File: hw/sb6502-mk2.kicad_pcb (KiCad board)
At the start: 2 copper layers, 160 x 120 mm, 66 parts, among them J1 Conn_01x03_Pin, J10 Conn_01x04_Socket, J11 Conn_01x04_Socket, J12 Conn_01x08_Socket, J13 Conn_01x08_Socket, J14 Conn_01x08_Socket, J15 Conn_01x08_Socket, J16 Conn_01x08_Socket, J17 Conn_01x04_Socket, J18 Conn_01x04_Socket, J19 Conn_01x02_Socket, J2 Conn_01x03_Pin, J20 Barrel_Jack, J21 Conn_01x02_Socket, J3 DE9_Receptacle, J4 Conn_01x08_Socket, J5 Conn_01x02_Socket, J6 Conn_01x08_Socket, J7 Conn_01x02_Socket, J8 Conn_01x07_Socket, J9 Conn_01x16_Socket, SW1 SW_Push, U1 TC1213, U10 W65C22NxP, U11 74HC138, U2 W65C02SxP, U3 74HC273, U4 ATF22V10, U5 ATF22V10, U6 HM628128, U7 AT28C256, U8 MC68B50, U9 MAX232, X1 1.8432 MHz

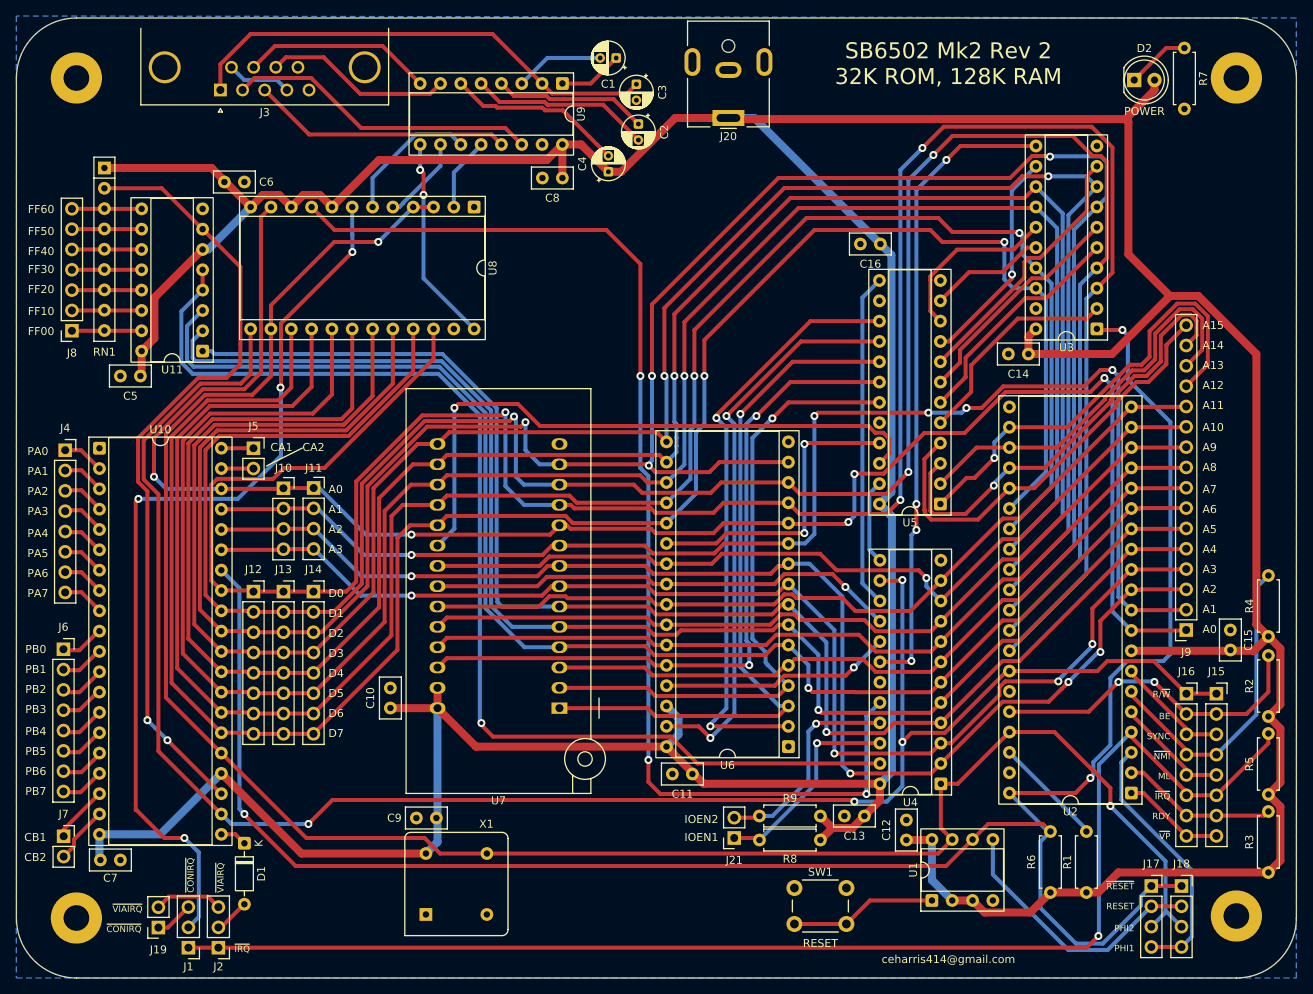
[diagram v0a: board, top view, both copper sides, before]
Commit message: additional pin sockets
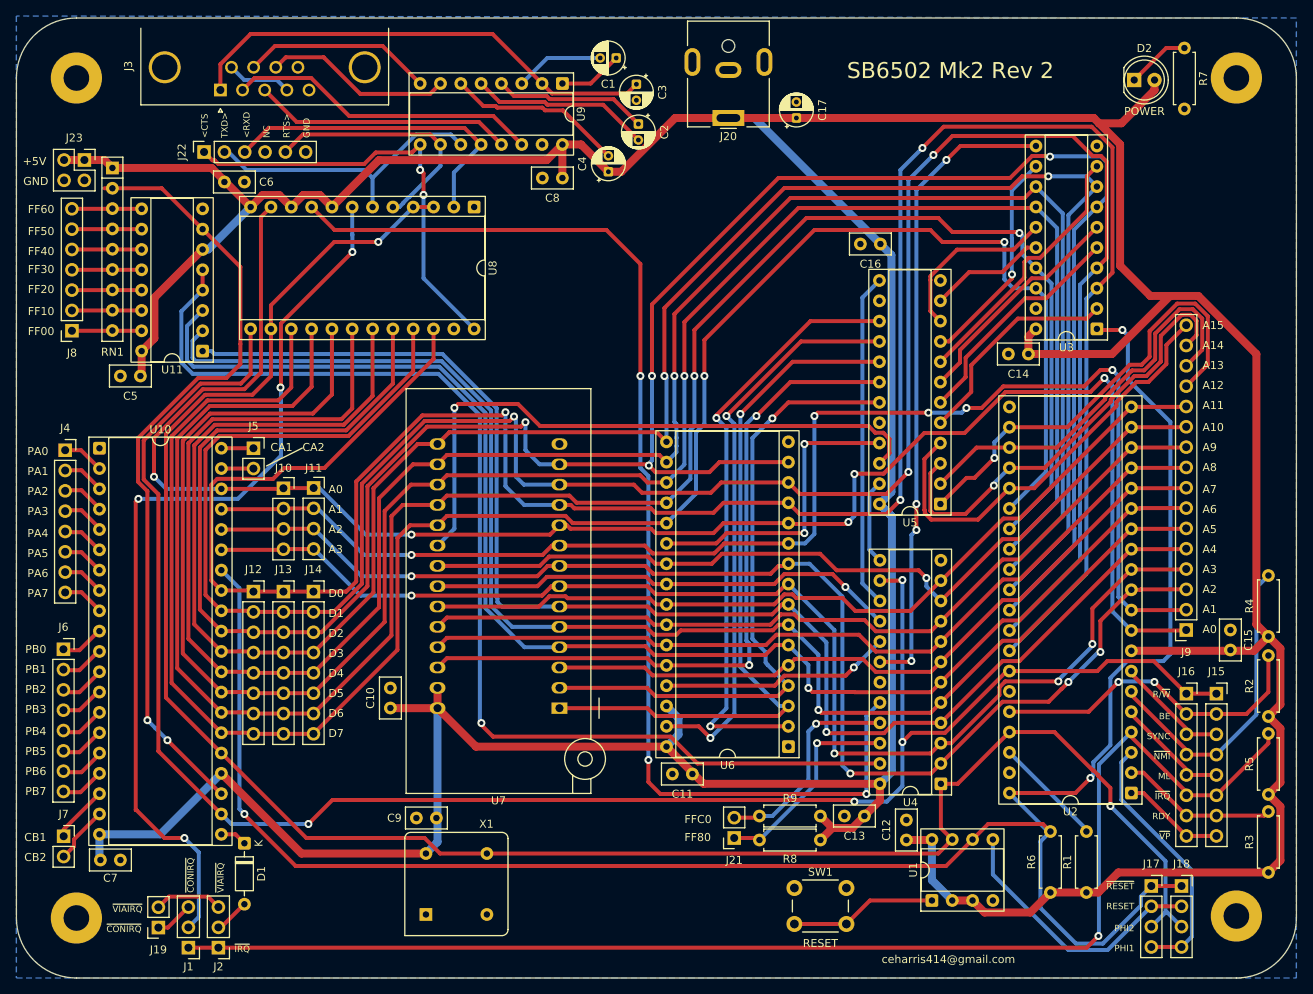
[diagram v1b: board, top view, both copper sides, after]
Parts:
- added C17: 10µF, Capacitor_THT:CP_Radial_D4.0mm_P2.00mm, F.Cu at (122.5, 37.5)
- added J22: Conn_01x06_Socket, Connector_PinSocket_2.54mm:PinSocket_1x06_P2.54mm_Vertical, F.Cu at (48.5, 41.8)
- added J23: Conn_02x02_Counter_Clockwise, Connector_PinSocket_2.54mm:PinSocket_2x02_P2.54mm_Vertical, F.Cu at (33.5, 42.8)
- moved RN1 1.00 mm to (37.0, 43.7)
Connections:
- net Net-(U8-Rx_Data) renamed /IO/RXD
- net Net-(U8-Tx_Data) renamed /IO/TXD
- net Net-(U8-~{CTS}) renamed /IO/CTS
- net Net-(U8-~{RTS}) renamed /IO/RTS
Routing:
- net /IO/RXD: track 9.23 -> 40.9 mm
- net /IO/CTS: track 26.1 -> 54.8 mm
- net /IO/RTS: track 10.8 -> 31.6 mm
- net /IO/TXD: track 17.4 -> 37.3 mm
- net VCC: track 636.4 -> 645.0 mm
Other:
- board text added: "+5V"
- board text added: "<CTS"
- board text added: "<RXD"
- board text added: "FF80"
- board text added: "FFC0"
- board text added: "GND"
- board text added: "NC"
- board text added: "RTS>"
- board text added: "SB6502 Mk2 Rev 2"
- board text added: "TXD>"
- board text removed: "IOEN1"
- board text removed: "IOEN2"
- board text removed: "SB6502 Mk2 Rev 2 32K ROM, 128K RAM"

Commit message: remove unnecessary pullups
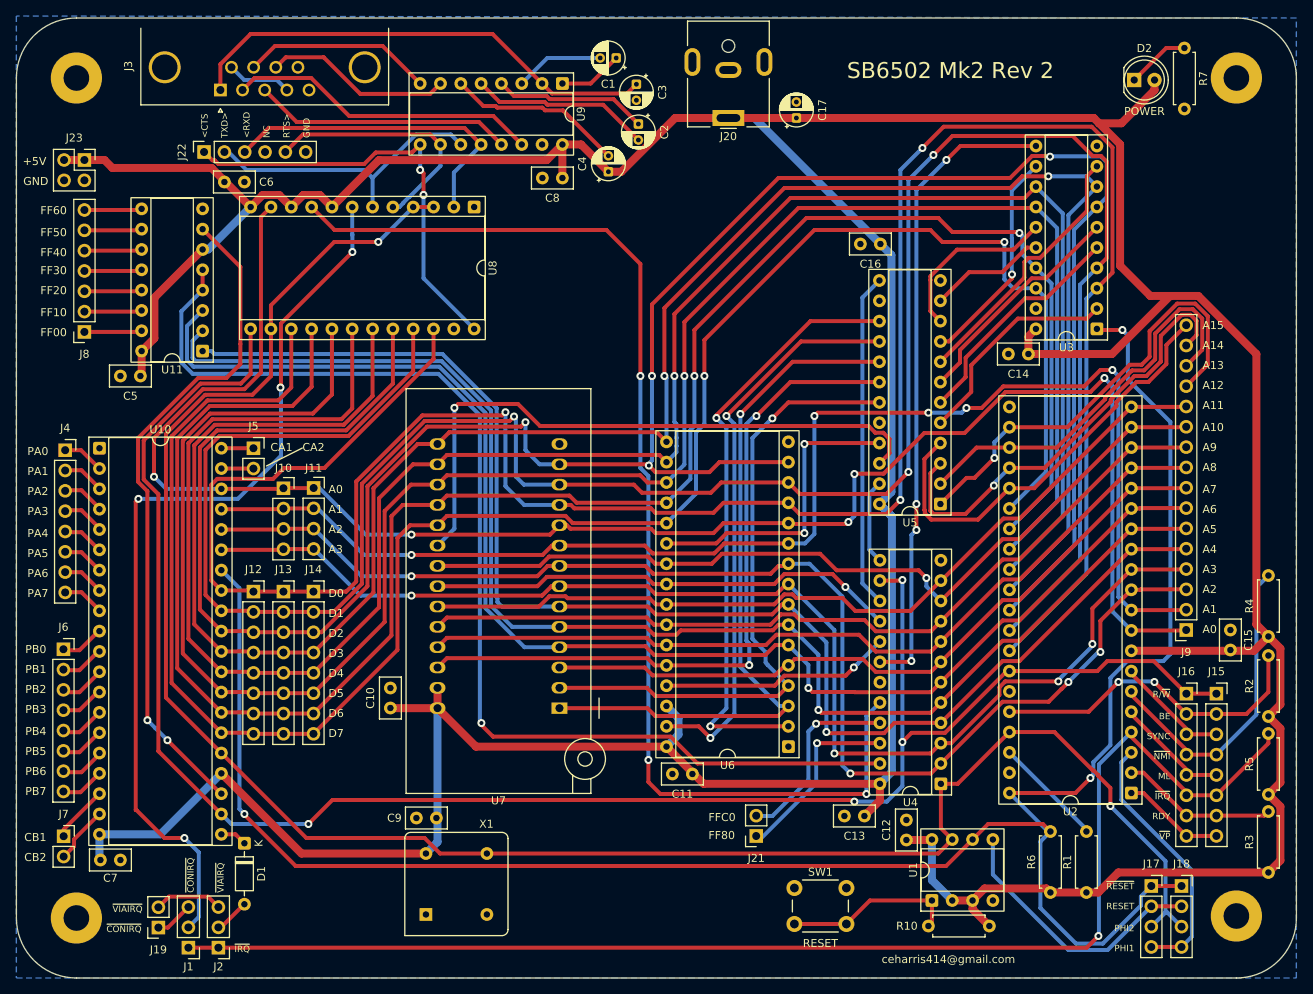
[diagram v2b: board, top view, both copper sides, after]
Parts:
- removed R8, R9: 3K, Resistor_THT:R_Axial_DIN0207_L6.3mm_D2.5mm_P7.62mm_Horizontal
- removed RN1: R_Network08_US, Resistor_THT:R_Array_SIP9
- added R10: 10K, Resistor_THT:R_Axial_DIN0207_L6.3mm_D2.5mm_P7.62mm_Horizontal, F.Cu at (146.6, 138.5)
- moved J21 2.76 mm to (117.5, 127.2)
- moved J8 1.57 mm to (33.5, 64.2)
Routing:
- net Net-(U10-~{CS2}): track 98.6 -> 84.2 mm
- net VCC: track 645.0 -> 639.3 mm
- net Net-(U1-~{PBRST}): track 18.4 -> 22.3 mm
- net /Decode/~{IOE1}: track 26.2 -> 22.9 mm
- net /Decode/~{IOE2}: track 26.8 -> 23.6 mm
- net Net-(J8-Pin_6): track 8.71 -> 7.22 mm
- net Net-(J8-Pin_5): track 8.71 -> 7.22 mm
- net Net-(J8-Pin_4): track 8.71 -> 7.22 mm
- net Net-(J8-Pin_3): track 8.71 -> 7.22 mm
- net Net-(J8-Pin_1): track 8.71 -> 7.22 mm
- net Net-(J8-Pin_7): track 8.71 -> 7.22 mm
- net Net-(J8-Pin_2): track 8.71 -> 7.22 mm
